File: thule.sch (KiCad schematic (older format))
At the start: 34 parts, among them J1 Conn_01x06, J2 USB_A, SW1 ~RST~, SW2 USR, U1 EFR32MG21x, U2 MIC5219-3.3YM5, U3 CP2102N-A01-GQFN24, Y1 32.768Khz, Y2 38.4Mhz

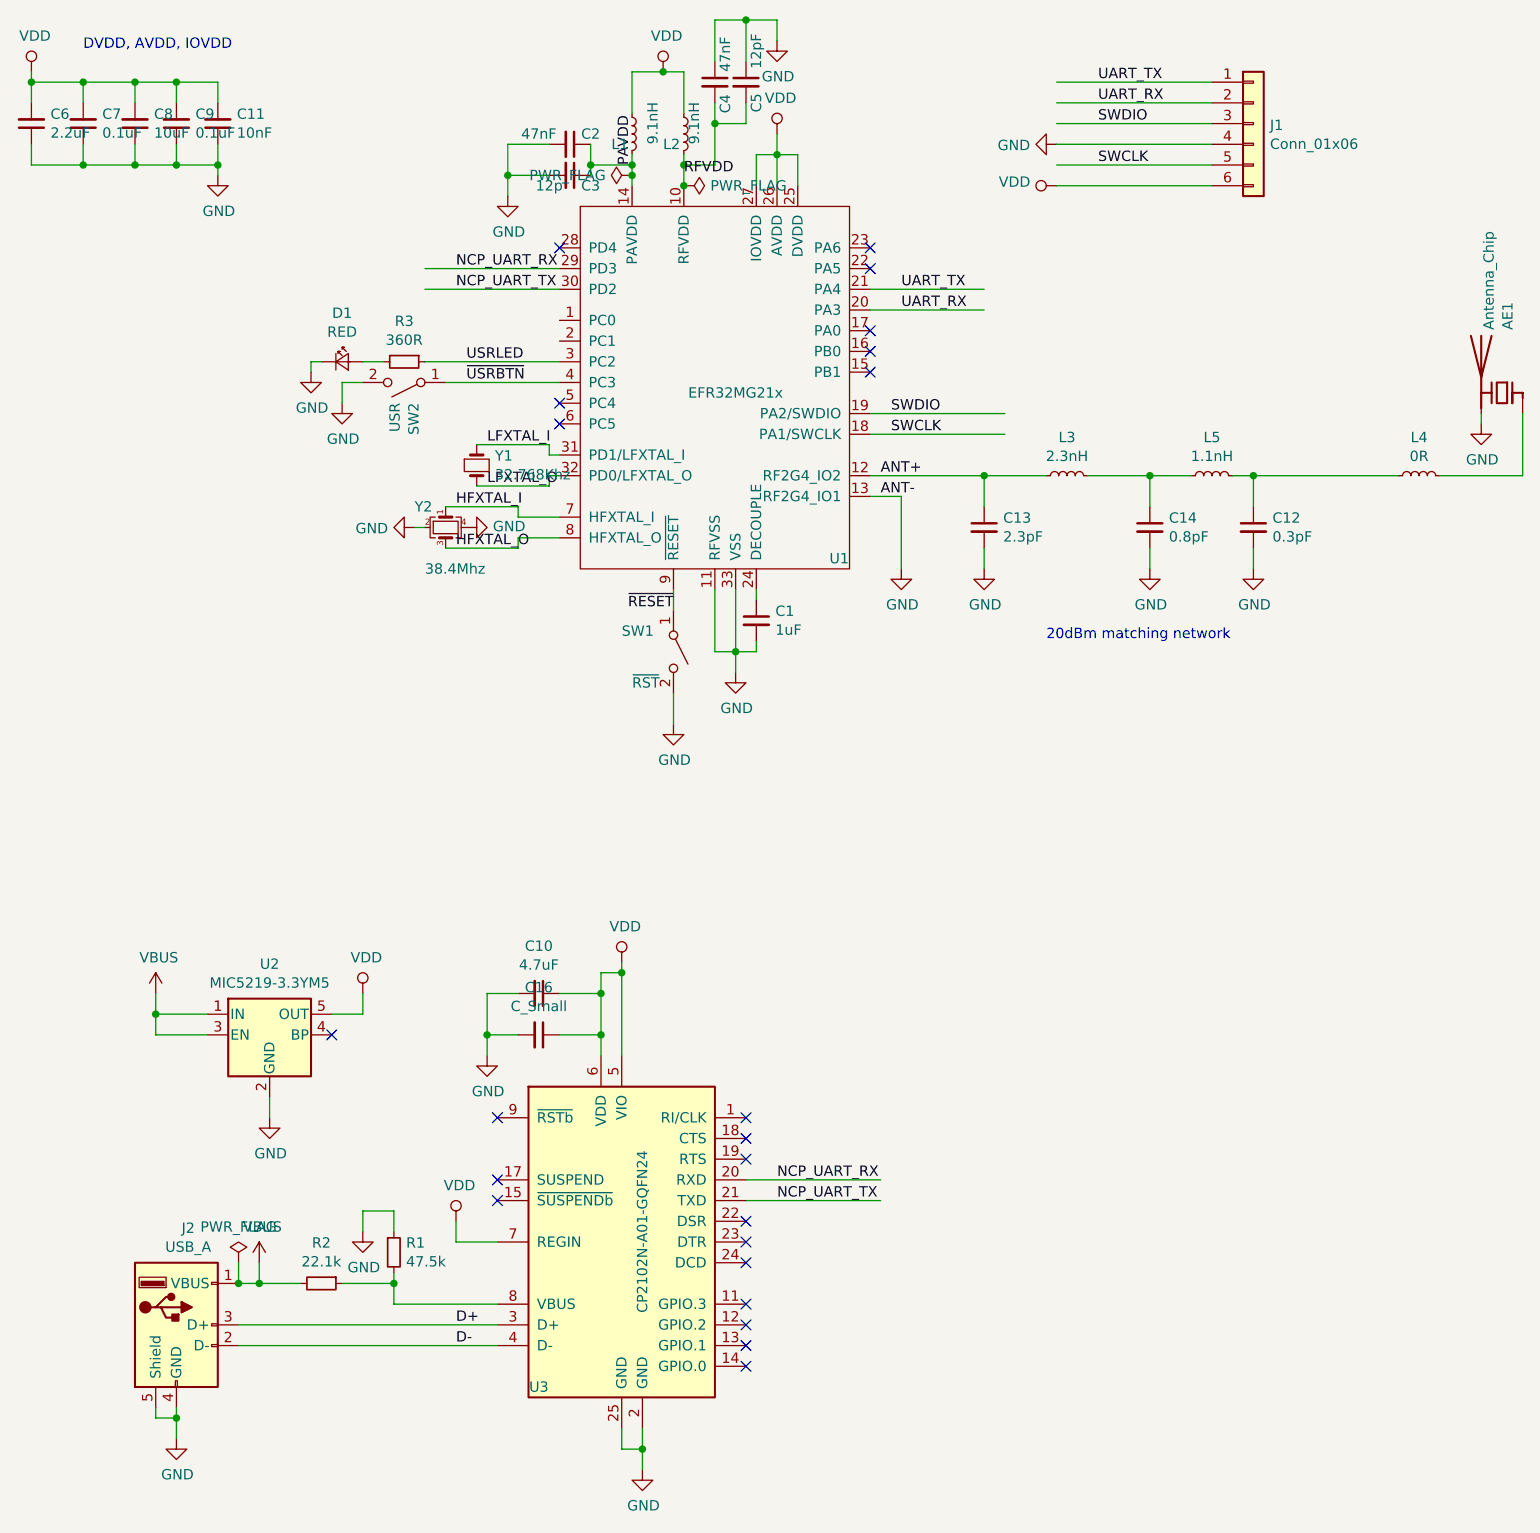
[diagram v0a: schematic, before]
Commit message: Start routing, use bigger packages
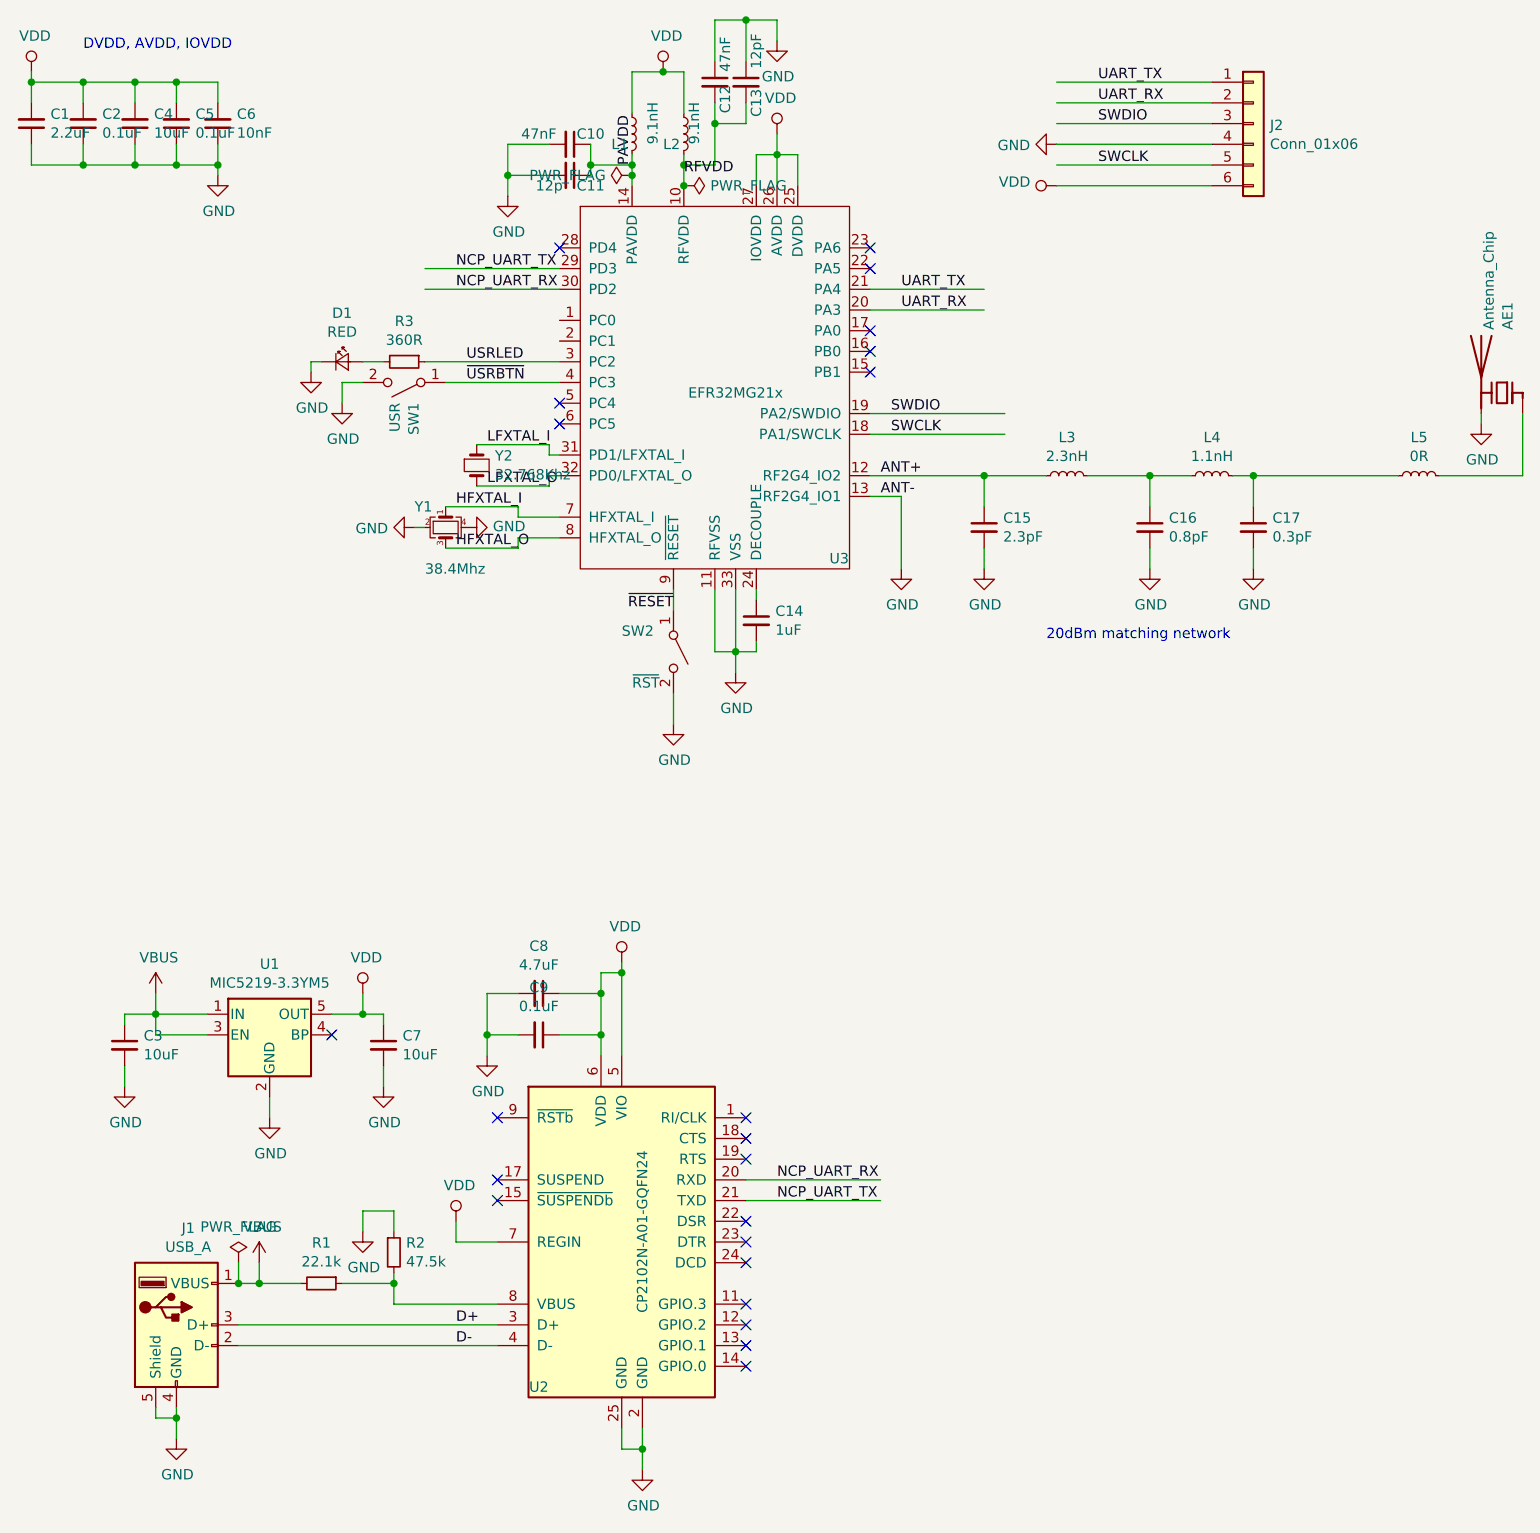
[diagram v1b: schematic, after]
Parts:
- added C3, C7: 10uF, Capacitor_SMD:C_0603_1608Metric, symbol Device:C_Small
- AE1: footprint RF_Antenna:Texas_SWRA117D_2.4GHz_Right -> Connector_Coaxial:SMA_Samtec_SMA-J-P-X-ST-EM1_EdgeMount; LCSC C127620 -> (none)
- C1: renamed from C6; footprint Capacitor_SMD:C_0402_1005Metric -> Capacitor_SMD:C_0603_1608Metric
- C10: renamed from C2; footprint Capacitor_SMD:C_0402_1005Metric -> Capacitor_SMD:C_0603_1608Metric
- C11: renamed from C3; footprint Capacitor_SMD:C_0402_1005Metric -> Capacitor_SMD:C_0603_1608Metric
- C12: renamed from C4; footprint Capacitor_SMD:C_0402_1005Metric -> Capacitor_SMD:C_0603_1608Metric
- C13: renamed from C5; footprint Capacitor_SMD:C_0402_1005Metric -> Capacitor_SMD:C_0603_1608Metric
- C14: renamed from C1; footprint Capacitor_SMD:C_0402_1005Metric -> Capacitor_SMD:C_0603_1608Metric
- C2: renamed from C7; footprint Capacitor_SMD:C_0402_1005Metric -> Capacitor_SMD:C_0603_1608Metric
- C4: renamed from C8; footprint Capacitor_SMD:C_0402_1005Metric -> Capacitor_SMD:C_0603_1608Metric
- C5: renamed from C9; footprint Capacitor_SMD:C_0402_1005Metric -> Capacitor_SMD:C_0603_1608Metric
- C6: renamed from C11; footprint Capacitor_SMD:C_0402_1005Metric -> Capacitor_SMD:C_0603_1608Metric
- C8: renamed from C10; footprint Capacitor_SMD:C_0402_1005Metric -> Capacitor_SMD:C_0603_1608Metric
- C9: renamed from C16; value C_Small -> 0.1uF; footprint Capacitor_SMD:C_0402_1005Metric -> Capacitor_SMD:C_0603_1608Metric
- D1: footprint LED_SMD:LED_0402_1005Metric -> LED_SMD:LED_0603_1608Metric
- J2: renamed from J1; footprint Connector_PinHeader_1.27mm:PinHeader_1x06_P1.27mm_Vertical -> Connector_PinHeader_2.54mm:PinHeader_1x06_P2.54mm_Vertical
- R1: renamed from R2; footprint Resistor_SMD:R_0402_1005Metric -> Resistor_SMD:R_0603_1608Metric
- R2: renamed from R1; footprint Resistor_SMD:R_0402_1005Metric -> Resistor_SMD:R_0603_1608Metric
- R3: footprint Resistor_SMD:R_0402_1005Metric -> Resistor_SMD:R_0603_1608Metric
- renumbered C13 to C15, C14 to C16, C12 to C17, J2 to J1, L5 to L4, L4 to L5, SW2 to SW1, SW1 to SW2, U2 to U1, U3 to U2, U1 to U3, Y2 to Y1, Y1 to Y2
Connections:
- wire segments 154 -> 160
